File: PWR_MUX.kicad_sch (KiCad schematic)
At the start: 9 parts, among them Q1 MMBT2222A, Q2 MMBT2222A, Q5 SQ3481CEV-T1_GE3, Q7 SQ3481CEV-T1_GE3

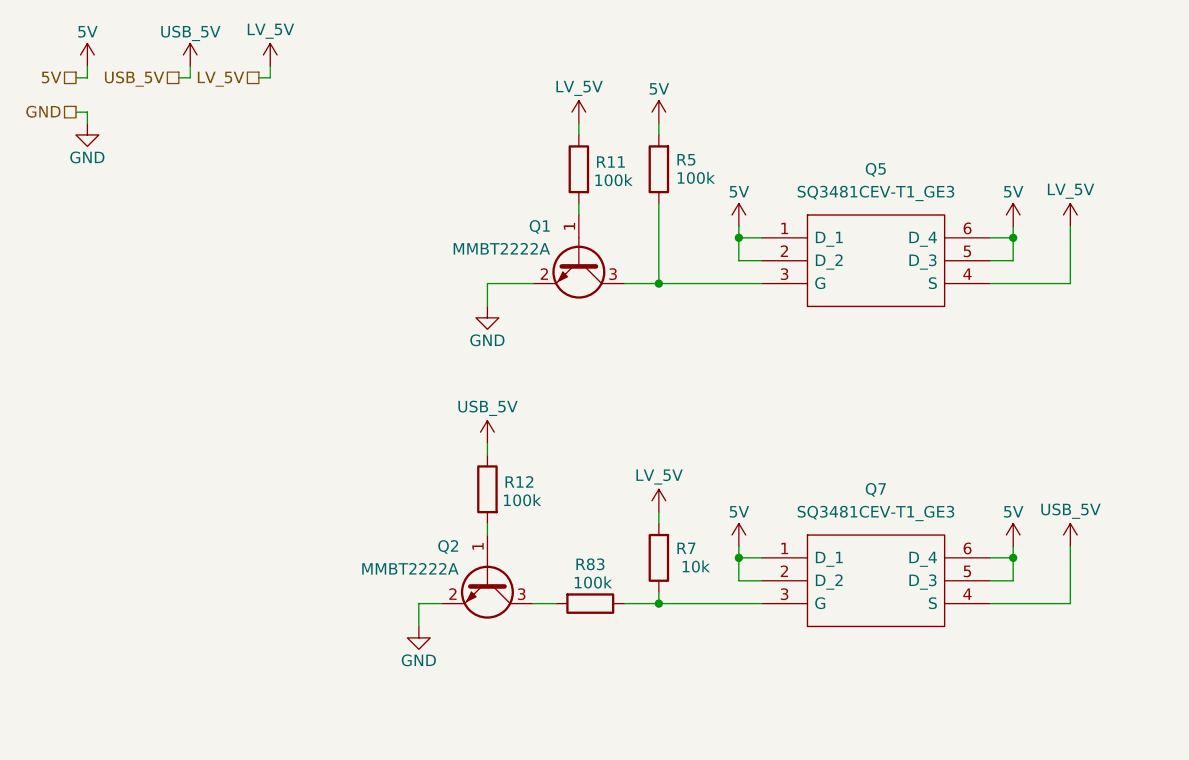
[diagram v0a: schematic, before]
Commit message: power mux
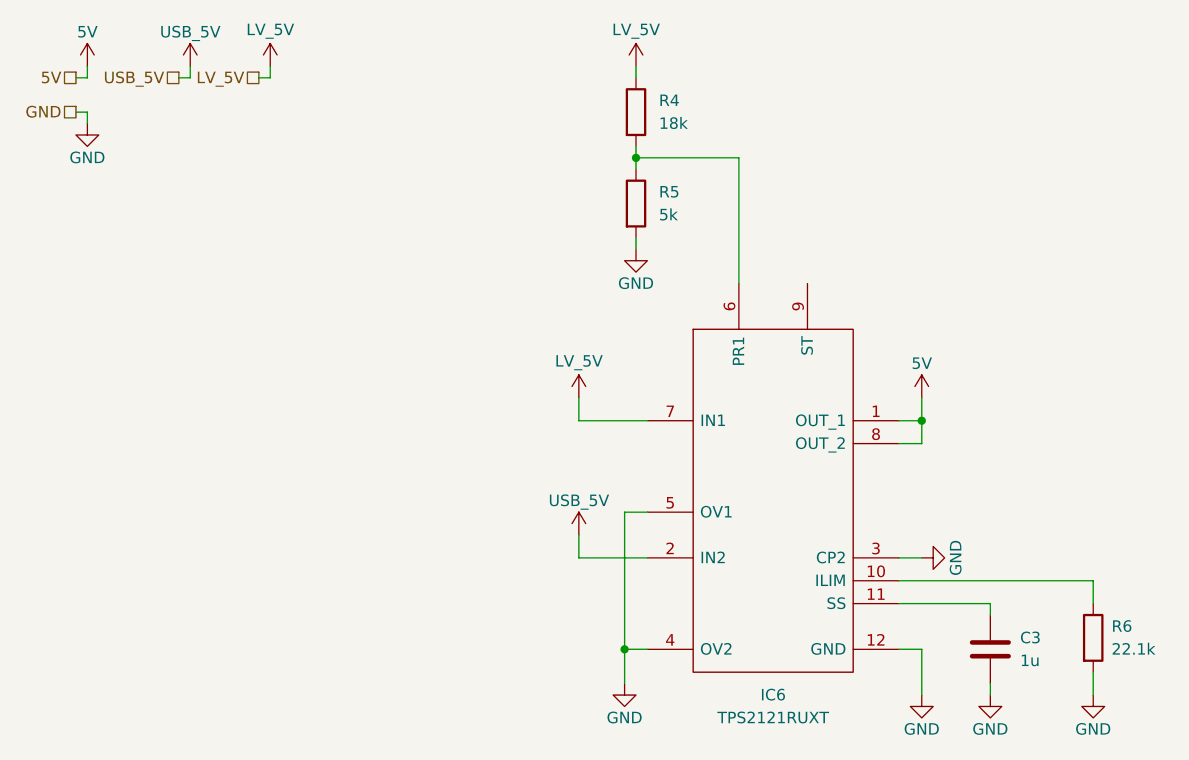
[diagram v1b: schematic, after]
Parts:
- removed Q1, Q2: MMBT2222A, Package_TO_SOT_SMD:SOT-23, symbol Transistor_BJT:MMBT2222A
- removed Q5, Q7: SQ3481CEV-T1_GE3, SOT95P284X110-6N, symbol 0_SamacSys_Parts:SQ3481CEV-T1_GE3
- removed R11, R12, R83: 100k, Resistor_SMD:R_0603_1608Metric_Pad0.98x0.95mm_HandSolder, symbol Device:R
- removed R7: 10k, Resistor_SMD:R_0603_1608Metric_Pad0.98x0.95mm_HandSolder, symbol Device:R
- added C3: 1u, Capacitor_SMD:C_0603_1608Metric_Pad1.08x0.95mm_HandSolder, symbol Device:C
- added IC6: TPS2121RUXT, TPS2121RUXT, symbol 0_SamacSys_Parts:TPS2121RUXT
- added R4: 18k, Resistor_SMD:R_0603_1608Metric_Pad0.98x0.95mm_HandSolder, symbol Device:R
- added R6: 22.1k, Resistor_SMD:R_0603_1608Metric_Pad0.98x0.95mm_HandSolder, symbol Device:R
- R5: value 100k -> 5k
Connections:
- net 5V: now also IC6.1 (OUT_1), IC6.8 (OUT_2); no longer R5.2
- net GND: now also R5.2, C3.2, IC6.12 (GND), IC6.3 (CP2), IC6.4 (OV2), IC6.5 (OV1), R6.2
- net LV_5V: now also IC6.7 (IN1), R4.1
- net USB_5V: now also IC6.2 (IN2)
- net at R5.1: now also IC6.6 (PR1), R4.2
- new net: C3.1, IC6.11 (SS)
- new net: IC6.10 (ILIM), R6.1

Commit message: added dip switches to wireless disables
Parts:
- added R47: 18k, Resistor_SMD:R_0603_1608Metric_Pad0.98x0.95mm_HandSolder, symbol Device:R
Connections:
- net USB_PWR_ST: now reaches IC6.9 (ST)
- net USB_PWR_ST: now also R47.2
- new net 3V3: R47.1

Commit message: redid annotations, added test point
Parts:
- renumbered C3 to C81, IC6 to IC7, R4 to R82, R5 to R83, R47 to R84, R6 to R85
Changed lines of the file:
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@@
 		(on_board yes)
 		(dnp no)
-		(property "Reference" "C3"
+		(property "Reference" "C81"
 			(at 125.222 85.09 0)
 			(effects
@@
 			(project ""
 				(path "/3aee14c3-5480-4f7c-989e-3fef81779034/05e3be97-98f6-4518-a1a7-240d4da327e6/d1a8c66e-d7c5-4f43-8cdd-a3ddabbe33e6"
-					(reference "C3")
+					(reference "C81")
 					(unit 1)
 				)
@@
 		(dnp no)
 		(fields_autoplaced yes)
-		(property "Reference" "R47"
+		(property "Reference" "R84"
 			(at 104.14 38.0999 0)
 			(effects
@@
 			(project "NCU"
 				(path "/3aee14c3-5480-4f7c-989e-3fef81779034/05e3be97-98f6-4518-a1a7-240d4da327e6/d1a8c66e-d7c5-4f43-8cdd-a3ddabbe33e6"
-					(reference "R47")
+					(reference "R84")
 					(unit 1)
 				)
@@
 		(on_board yes)
 		(dnp no)
-		(property "Reference" "#PWR0292"
+		(property "Reference" "#PWR0303"
 			(at 82.55 48.26 0)
 			(effects
@@
 			(project "NCU"
 				(path "/3aee14c3-5480-4f7c-989e-3fef81779034/05e3be97-98f6-4518-a1a7-240d4da327e6/d1a8c66e-d7c5-4f43-8cdd-a3ddabbe33e6"
-					(reference "#PWR0292")
+					(reference "#PWR0303")
 					(unit 1)
 				)
@@
 		(on_board yes)
 		(dnp no)
-		(property "Reference" "#PWR0286"
+		(property "Reference" "#PWR0306"
 			(at 120.65 76.2 0)
 			(effects
@@
 			(project "NCU"
 				(path "/3aee14c3-5480-4f7c-989e-3fef81779034/05e3be97-98f6-4518-a1a7-240d4da327e6/d1a8c66e-d7c5-4f43-8cdd-a3ddabbe33e6"
-					(reference "#PWR0286")
+					(reference "#PWR0306")
 					(unit 1)
 				)
@@
 		(on_board yes)
 		(dnp no)
-		(property "Reference" "#PWR0284"
+		(property "Reference" "#PWR0294"
 			(at 21.59 25.4 0)
 			(effects
@@
 			(project "NCU"
 				(path "/3aee14c3-5480-4f7c-989e-3fef81779034/05e3be97-98f6-4518-a1a7-240d4da327e6/d1a8c66e-d7c5-4f43-8cdd-a3ddabbe33e6"
-					(reference "#PWR0284")
+					(reference "#PWR0294")
 					(unit 1)
 				)
@@
 		(on_board yes)
 		(dnp no)
-		(property "Reference" "#PWR0294"
+		(property "Reference" "#PWR0308"
 			(at 121.92 97.79 0)
 			(effects
@@
 			(project "NCU"
 				(path "/3aee14c3-5480-4f7c-989e-3fef81779034/05e3be97-98f6-4518-a1a7-240d4da327e6/d1a8c66e-d7c5-4f43-8cdd-a3ddabbe33e6"
-					(reference "#PWR0294")
+					(reference "#PWR0308")
 					(unit 1)
 				)
@@
 		(on_board yes)
 		(dnp no)
-		(property "Reference" "#PWR0309"
+		(property "Reference" "#PWR0304"
 			(at 101.6 36.83 0)
 			(effects
@@
 			(project "NCU"
 				(path "/3aee14c3-5480-4f7c-989e-3fef81779034/05e3be97-98f6-4518-a1a7-240d4da327e6/d1a8c66e-d7c5-4f43-8cdd-a3ddabbe33e6"
-					(reference "#PWR0309")
+					(reference "#PWR0304")
 					(unit 1)
 				)
@@
 		(on_board yes)
 		(dnp no)
-		(property "Reference" "#PWR0282"
+		(property "Reference" "#PWR0307"
 			(at 114.3 97.79 0)
 			(effects
@@
 			(project "NCU"
 				(path "/3aee14c3-5480-4f7c-989e-3fef81779034/05e3be97-98f6-4518-a1a7-240d4da327e6/d1a8c66e-d7c5-4f43-8cdd-a3ddabbe33e6"
-					(reference "#PWR0282")
+					(reference "#PWR0307")
 					(unit 1)
 				)
@@
 		(on_board yes)
 		(dnp no)
-		(property "Reference" "R6"
+		(property "Reference" "R85"
 			(at 135.382 83.82 0)
 			(effects
@@
 			(project "NCU"
 				(path "/3aee14c3-5480-4f7c-989e-3fef81779034/05e3be97-98f6-4518-a1a7-240d4da327e6/d1a8c66e-d7c5-4f43-8cdd-a3ddabbe33e6"
-					(reference "R6")
+					(reference "R85")
 					(unit 1)
 				)
@@
 		(on_board yes)
 		(dnp no)
-		(property "Reference" "#PWR0291"
+		(property "Reference" "#PWR0302"
 			(at 82.55 25.4 0)
 			(effects
@@
 			(project "NCU"
 				(path "/3aee14c3-5480-4f7c-989e-3fef81779034/05e3be97-98f6-4518-a1a7-240d4da327e6/d1a8c66e-d7c5-4f43-8cdd-a3ddabbe33e6"
-					(reference "#PWR0291")
+					(reference "#PWR0302")
 					(unit 1)
 				)
@@
 		(on_board yes)
 		(dnp no)
-		(property "Reference" "#PWR0293"
+		(property "Reference" "#PWR0309"
 			(at 133.35 97.79 0)
 			(effects
@@
 			(project "NCU"
 				(path "/3aee14c3-5480-4f7c-989e-3fef81779034/05e3be97-98f6-4518-a1a7-240d4da327e6/d1a8c66e-d7c5-4f43-8cdd-a3ddabbe33e6"
-					(reference "#PWR0293")
+					(reference "#PWR0309")
 					(unit 1)
 				)
@@
 		(dnp no)
 		(fields_autoplaced yes)
-		(property "Reference" "R5"
+		(property "Reference" "R83"
 			(at 85.09 35.5599 0)
 			(effects
@@
 			(project "NCU"
 				(path "/3aee14c3-5480-4f7c-989e-3fef81779034/05e3be97-98f6-4518-a1a7-240d4da327e6/d1a8c66e-d7c5-4f43-8cdd-a3ddabbe33e6"
-					(reference "R5")
+					(reference "R83")
 					(unit 1)
 				)
@@
 		(on_board yes)
 		(dnp no)
-		(property "Reference" "#PWR090"
+		(property "Reference" "#PWR0298"
 			(at 49.53 25.4 0)
 			(effects
@@
 			(project "NCU"
 				(path "/3aee14c3-5480-4f7c-989e-3fef81779034/05e3be97-98f6-4518-a1a7-240d4da327e6/d1a8c66e-d7c5-4f43-8cdd-a3ddabbe33e6"
-					(reference "#PWR090")
+					(reference "#PWR0298")
 					(unit 1)
 				)
@@
 		(on_board yes)
 		(dnp no)
-		(property "Reference" "#PWR0288"
+		(property "Reference" "#PWR0297"
 			(at 41.91 25.4 0)
 			(effects
@@
 			(project "NCU"
 				(path "/3aee14c3-5480-4f7c-989e-3fef81779034/05e3be97-98f6-4518-a1a7-240d4da327e6/d1a8c66e-d7c5-4f43-8cdd-a3ddabbe33e6"
-					(reference "#PWR0288")
+					(reference "#PWR0297")
 					(unit 1)
 				)
@@
 		(dnp no)
 		(fields_autoplaced yes)
-		(property "Reference" "R4"
+		(property "Reference" "R82"
 			(at 85.09 25.3999 0)
 			(effects
@@
 			(project ""
 				(path "/3aee14c3-5480-4f7c-989e-3fef81779034/05e3be97-98f6-4518-a1a7-240d4da327e6/d1a8c66e-d7c5-4f43-8cdd-a3ddabbe33e6"
-					(reference "R4")
+					(reference "R82")
 					(unit 1)
 				)
@@
 		(dnp no)
 		(fields_autoplaced yes)
-		(property "Reference" "IC6"
+		(property "Reference" "IC7"
 			(at 97.79 91.44 0)
 			(effects
@@
 			(project ""
 				(path "/3aee14c3-5480-4f7c-989e-3fef81779034/05e3be97-98f6-4518-a1a7-240d4da327e6/d1a8c66e-d7c5-4f43-8cdd-a3ddabbe33e6"
-					(reference "IC6")
+					(reference "IC7")
 					(unit 1)
 				)
@@
 		(on_board yes)
 		(dnp no)
-		(property "Reference" "#PWR055"
+		(property "Reference" "#PWR0299"
 			(at 76.2 62.23 0)
 			(effects
@@
 			(project "NCU"
 				(path "/3aee14c3-5480-4f7c-989e-3fef81779034/05e3be97-98f6-4518-a1a7-240d4da327e6/d1a8c66e-d7c5-4f43-8cdd-a3ddabbe33e6"
-					(reference "#PWR055")
+					(reference "#PWR0299")
 					(unit 1)
 				)
@@
 		(on_board yes)
 		(dnp no)
-		(property "Reference" "#PWR0287"
+		(property "Reference" "#PWR0296"
 			(at 33.02 25.4 0)
 			(effects
@@
 			(project "NCU"
 				(path "/3aee14c3-5480-4f7c-989e-3fef81779034/05e3be97-98f6-4518-a1a7-240d4da327e6/d1a8c66e-d7c5-4f43-8cdd-a3ddabbe33e6"
-					(reference "#PWR0287")
+					(reference "#PWR0296")
 					(unit 1)
 				)
@@
 		(on_board yes)
 		(dnp no)
-		(property "Reference" "#PWR0285"
+		(property "Reference" "#PWR0301"
 			(at 81.28 96.52 0)
 			(effects
@@
 			(project "NCU"
 				(path "/3aee14c3-5480-4f7c-989e-3fef81779034/05e3be97-98f6-4518-a1a7-240d4da327e6/d1a8c66e-d7c5-4f43-8cdd-a3ddabbe33e6"
-					(reference "#PWR0285")
+					(reference "#PWR0301")
 					(unit 1)
 				)
@@
 		(on_board yes)
 		(dnp no)
-		(property "Reference" "#PWR0283"
+		(property "Reference" "#PWR0295"
 			(at 21.59 34.29 0)
 			(effects
@@
 			(project "NCU"
 				(path "/3aee14c3-5480-4f7c-989e-3fef81779034/05e3be97-98f6-4518-a1a7-240d4da327e6/d1a8c66e-d7c5-4f43-8cdd-a3ddabbe33e6"
-					(reference "#PWR0283")
+					(reference "#PWR0295")
 					(unit 1)
 				)
@@
 		(on_board yes)
 		(dnp no)
-		(property "Reference" "#PWR057"
+		(property "Reference" "#PWR0305"
 			(at 114.3 62.23 0)
 			(effects
@@
 			(project "NCU"
 				(path "/3aee14c3-5480-4f7c-989e-3fef81779034/05e3be97-98f6-4518-a1a7-240d4da327e6/d1a8c66e-d7c5-4f43-8cdd-a3ddabbe33e6"
-					(reference "#PWR057")
+					(reference "#PWR0305")
 					(unit 1)
 				)
@@
 		(on_board yes)
 		(dnp no)
-		(property "Reference" "#PWR056"
+		(property "Reference" "#PWR0300"
 			(at 76.2 77.47 0)
 			(effects
@@
 			(project "NCU"
 				(path "/3aee14c3-5480-4f7c-989e-3fef81779034/05e3be97-98f6-4518-a1a7-240d4da327e6/d1a8c66e-d7c5-4f43-8cdd-a3ddabbe33e6"
-					(reference "#PWR056")
-					(unit 1)
-				)
+					(reference "#PWR0300")
+					(unit 1)
+				)
